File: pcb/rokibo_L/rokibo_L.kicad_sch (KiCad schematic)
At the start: 52 parts, among them SW000 SW_Push, SW001 SW_Push, SW002 SW_Push, SW003 SW_Push, SW004 SW_Push, SW005 SW_Push, SW006 SW_Push, SW007 SW_Push, SW008 SW_Push, SW009 SW_Push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

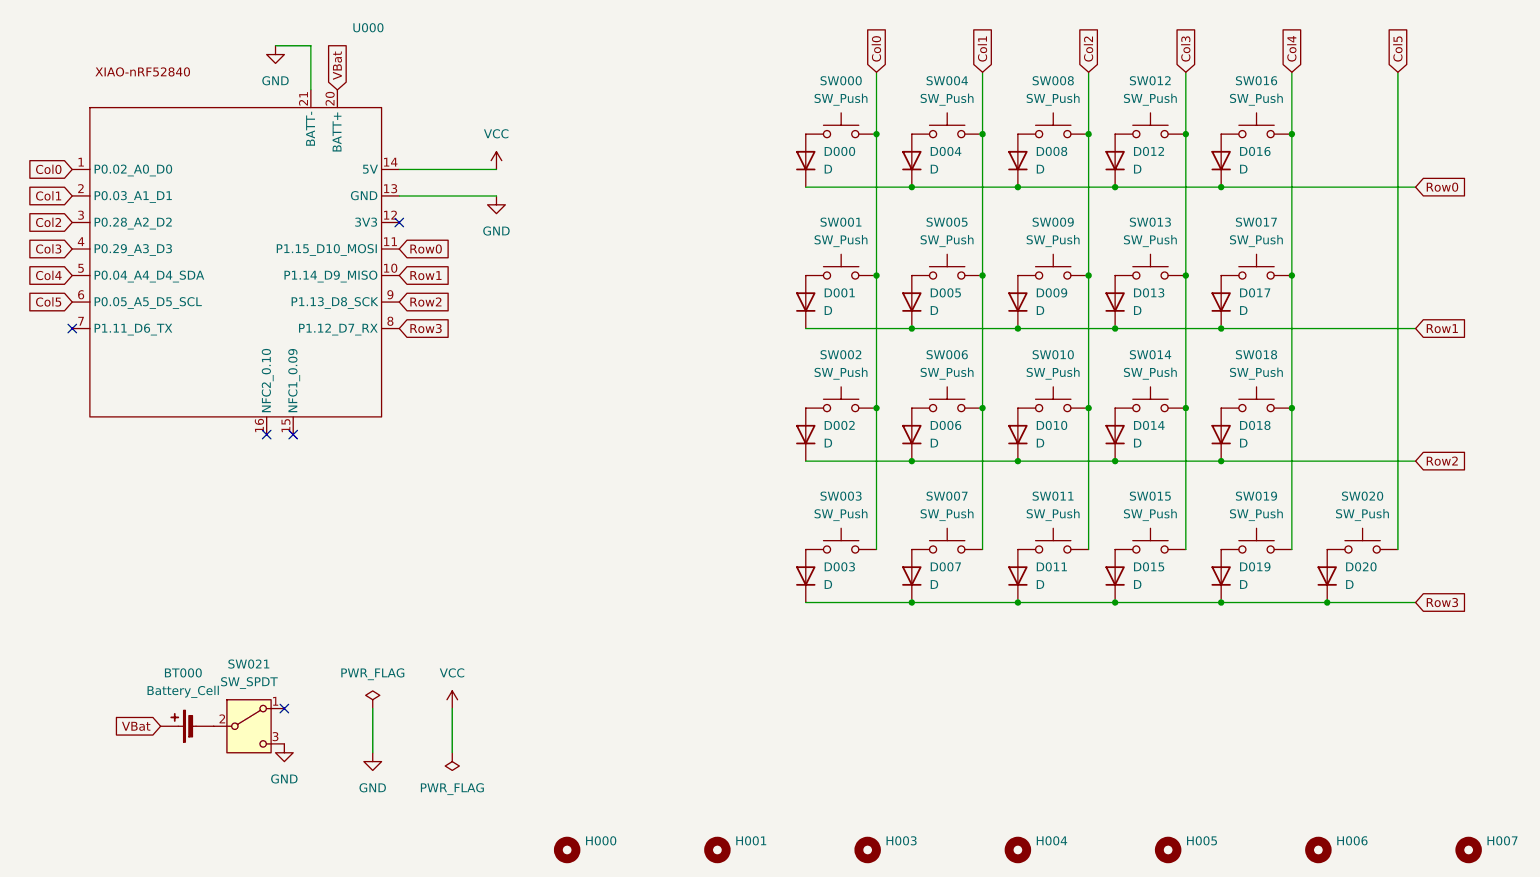
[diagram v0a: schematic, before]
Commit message: fix: Draw symmetric edge cut
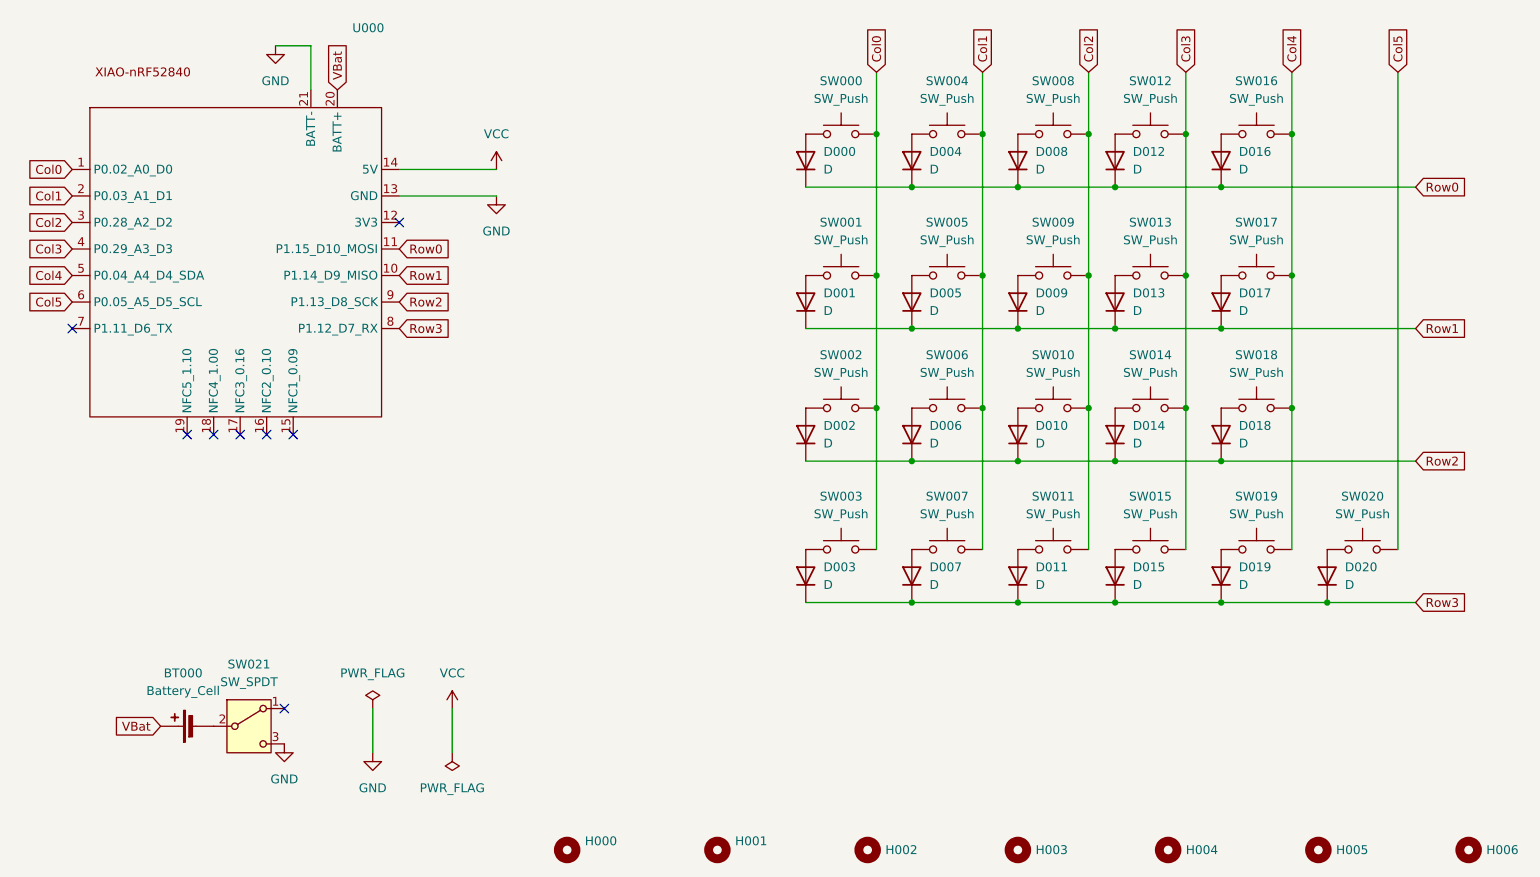
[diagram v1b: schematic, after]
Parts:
- removed U000: ~, roBa:XIAO_nRF52840_wBAT_wNFC, symbol roBa:XIAO-nRF52840
- added U000: ~, rokibo:XIAO_nRF52840_wBAT_wNFC, symbol rokibo:XIAO-nRF52840
- BT000: footprint roBa:JST_S2B-PH-SM4-TB -> rokibo:JST_S2B-PH-SM4-TB
- D000, D001, D002, D003, D004, D005, D006, D007, D008, D009, D010, D011, D012, D013, D014, D015, D016, D017, D018, D019, D020: footprint kbd_Parts:Diode_SMD -> rokibo:Diode_SMD
- H000, H001: footprint MountingHole:MountingHole_4.3mm_M4 -> rokibo:m2_Spacer_Hole
- H002: renamed from H003; footprint MountingHole:MountingHole_4.3mm_M4 -> rokibo:m2_Spacer_Hole
- H003: renamed from H004; footprint MountingHole:MountingHole_4.3mm_M4 -> rokibo:m2_Spacer_Hole
- H004: renamed from H005; footprint MountingHole:MountingHole_4.3mm_M4 -> rokibo:m2_Spacer_Hole
- H005: renamed from H006; footprint MountingHole:MountingHole_4.3mm_M4 -> rokibo:m2_Spacer_Hole
- H006: renamed from H007; footprint MountingHole:MountingHole_4.3mm_M4 -> rokibo:m2_Spacer_Hole
- SW021: footprint roBa:MSK-12C02 -> rokibo:TGSW_MSK-12D19
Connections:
- net Col0: now also U000.1 (P0.02_A0_D0)
- net Col1: now also U000.2 (P0.03_A1_D1)
- net Col2: now also U000.3 (P0.28_A2_D2)
- net Col3: now also U000.4 (P0.29_A3_D3)
- net Col4: now also U000.5 (P0.04_A4_D4_SDA)
- net Col5: now also U000.6 (P0.05_A5_D5_SCL)
- net GND: now also U000.13 (GND), U000.21 (BATT-)
- net Row0: now also U000.11 (P1.15_D10_MOSI)
- net Row1: now also U000.10 (P1.14_D9_MISO)
- net Row2: now also U000.9 (P1.13_D8_SCK)
- net Row3: now also U000.8 (P1.12_D7_RX)
- net VBat: now also U000.20 (BATT+)
- net VCC: now also U000.14 (5V)
- no-connect marks 5 -> 8

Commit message: feat: Draw left track
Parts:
- H000, H001, H002, H003, H004, H005, H006: value (none) -> ~
- U000: footprint rokibo:XIAO_nRF52840_wBAT_wNFC -> rokibo:XIAO_nRF52840_wBAT_wNFC_1
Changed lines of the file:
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@@
 			)
 		)
-		(property "Value" ""
+		(property "Value" "~"
 			(at 170.18 143.5099 0)
 			(effects
@@
 			)
 		)
-		(property "Value" ""
+		(property "Value" "~"
 			(at 256.54 143.5099 0)
 			(effects
@@
 			)
 		)
-		(property "Value" ""
+		(property "Value" "~"
 			(at 148.59 143.5099 0)
 			(effects
@@
 			)
 		)
-		(property "Footprint" "rokibo:XIAO_nRF52840_wBAT_wNFC"
+		(property "Footprint" "rokibo:XIAO_nRF52840_wBAT_wNFC_1"
 			(at 43.18 29.21 0)
 			(effects
@@
 			)
 		)
-		(property "Value" ""
+		(property "Value" "~"
 			(at 191.77 143.5099 0)
 			(effects
@@
 			)
 		)
-		(property "Value" ""
+		(property "Value" "~"
 			(at 213.36 143.5099 0)
 			(effects
@@
 			)
 		)
-		(property "Value" ""
+		(property "Value" "~"
 			(at 234.95 143.5099 0)
 			(effects
@@
 			)
 		)
-		(property "Value" ""
+		(property "Value" "~"
 			(at 127 143.5099 0)
 			(effects
